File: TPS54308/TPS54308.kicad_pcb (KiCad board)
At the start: 2 copper layers, 30.5 x 15.2 mm, 14 parts, among them P1 CONN_01X04, P2 CONN_01X04, U1 TPS54308DDC

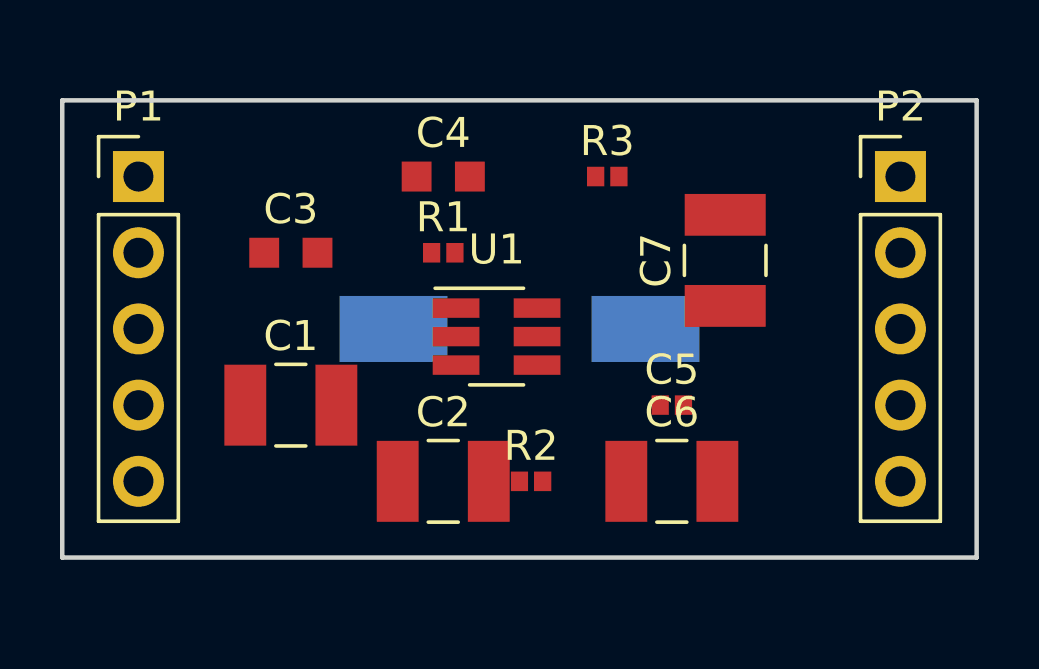
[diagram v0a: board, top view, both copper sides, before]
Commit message: placement draft
drafted placement of all components and started routing.
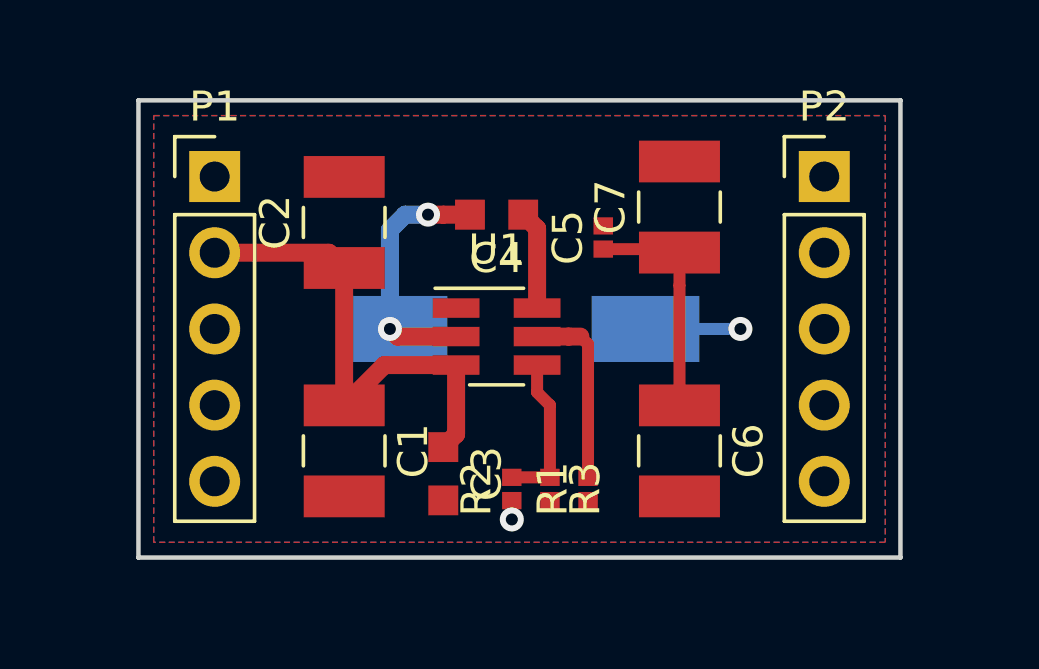
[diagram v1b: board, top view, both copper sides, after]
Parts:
- moved R3 10.6 mm to (110.2, 106.9), turned to 270 degrees
- moved C2 9.24 mm to (103.4, 98.1), turned to 90 degrees
- moved R1 9.24 mm to (111.5, 106.9), turned to 90 degrees
- moved C3 8.95 mm to (106.7, 106.4), turned to 270 degrees
- moved C5 6.04 mm to (112.0, 98.6), turned to 90 degrees
- moved P1 2.54 mm to (99.1, 96.5)
- moved P2 2.54 mm to (119.4, 96.5)
- moved C1 2.34 mm to (103.4, 105.7), turned to 270 degrees
- moved C7 2.34 mm to (114.6, 97.5)
- moved C4 2.18 mm to (108.5, 97.8), turned to 180 degrees
- moved C6 1.05 mm to (114.6, 105.7), turned to 270 degrees
- moved R2 0.69 mm to (109.0, 106.9), turned to 90 degrees
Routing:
- net VIN: track 0.00 -> 16.3 mm
- net VOUT: track 0.00 -> 11.5 mm, vias 0 -> 2
- net SW: track 0.00 -> 8.49 mm, vias 0 -> 2
- net EN: track 0.00 -> 6.24 mm
- net FB: track 0.00 -> 5.19 mm
- net BOOT: track 0.00 -> 3.31 mm
- added copper zone on B.Cu, net GND
- added copper zone on F.Cu, net GND
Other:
- board size 30.5 x 15.2 mm -> 25.4 x 15.2 mm

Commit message: size reduction
changed to 4pin pin headers, reduced board size, second placing attempt
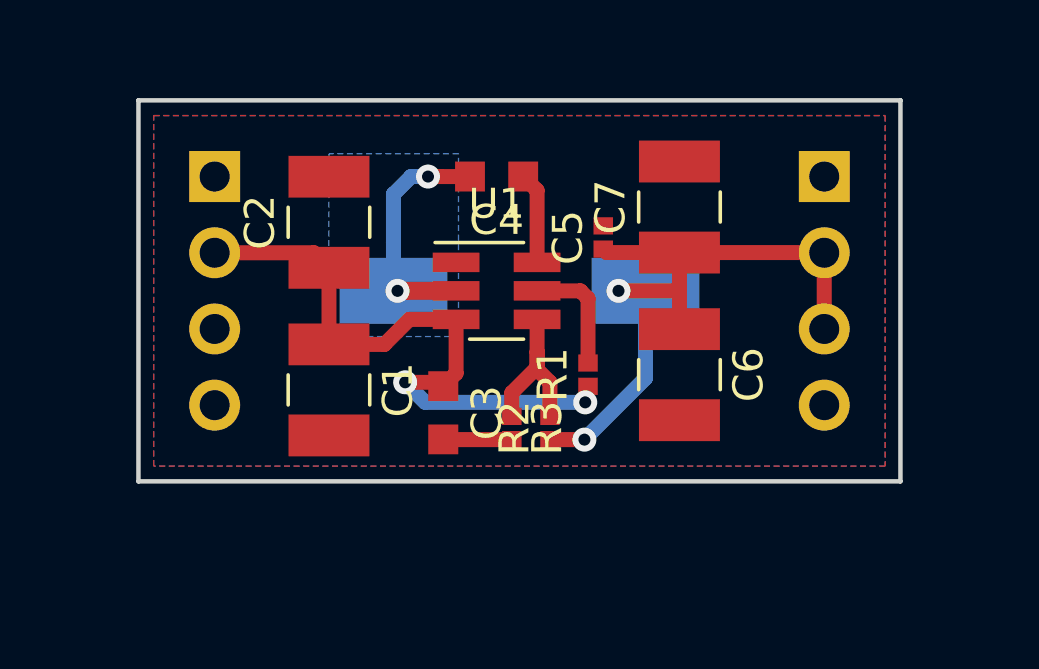
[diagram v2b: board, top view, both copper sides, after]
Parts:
- P1, P2: footprint Connector_PinHeader_2.54mm:PinHeader_1x05_P2.54mm_Vertical -> Connector_PinHeader_2.54mm:PinHeader_1x04_P2.54mm_Vertical; moved to B.Cu
- moved R1 3.81 mm to (111.5, 103.1)
- moved C6 2.54 mm to (114.6, 103.1)
- moved R2 2.40 mm to (110.2, 104.9)
- moved R3 2.40 mm to (109.0, 104.9)
- moved C1 2.09 mm to (102.9, 103.6)
- moved C3 2.03 mm to (106.7, 104.4)
- moved U1 1.52 mm to (108.5, 100.3)
- moved C4 1.27 mm to (108.5, 96.5)
- moved L1 1.27 mm to (109.2, 100.3)
- moved C2 0.51 mm to (102.9, 98.0)
- turned P1 to 180 degrees
- turned P2 to 180 degrees
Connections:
- P1 pad 3: EN -> GND
- P1 pad 4: GND -> EN
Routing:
- net VOUT: track 11.5 -> 22.7 mm
- net VIN: track 16.3 -> 21.8 mm, vias 0 -> 2
- net GND: track 0.00 -> 2.29 mm
- net EN: track 6.24 -> 3.96 mm
- net FB: track 5.19 -> 5.91 mm
- net SW: track 8.49 -> 7.97 mm
- added copper zone on B.Cu, net SW
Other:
- board size 25.4 x 15.2 mm -> 25.4 x 12.7 mm
- net class Default: trace_width 0.25 -> 0.5

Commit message: wired all connections
... additionally some copper fills and thermal vias
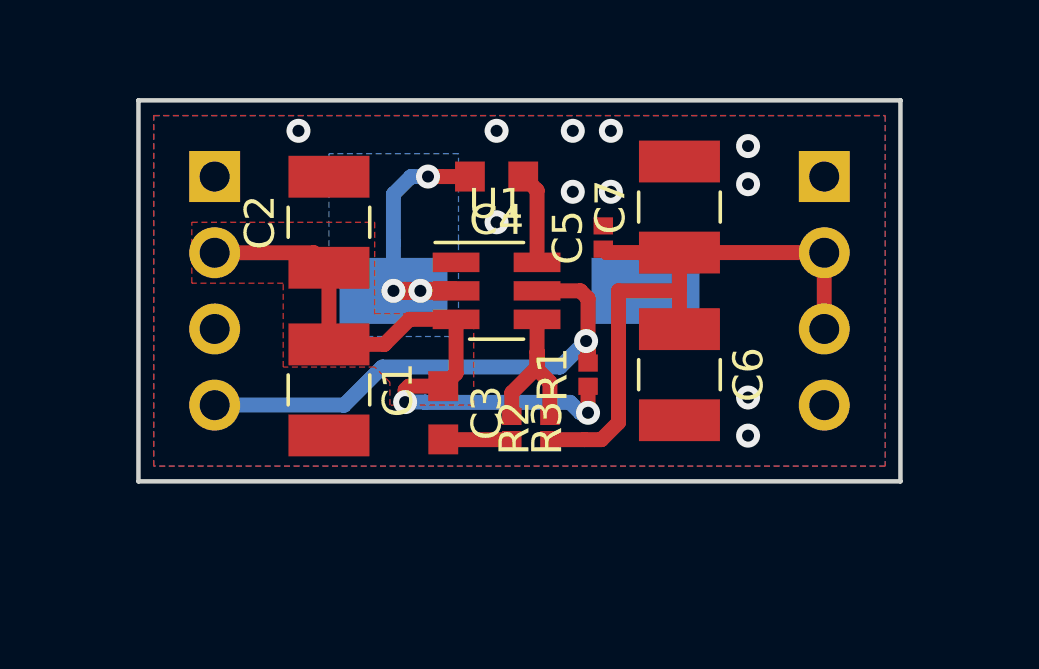
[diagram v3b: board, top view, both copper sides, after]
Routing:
- net EN: track 3.96 -> 18.1 mm, vias 0 -> 1
- net VIN: track 21.8 -> 22.7 mm
- net VOUT: vias 2 -> 0
- net SW: vias 2 -> 3
- net GND: vias 0 -> 11
- added copper zone on F.Cu, net VIN
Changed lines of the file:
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@@
   (general
     (thickness 1.6)
-    (drawings 4)
-    (tracks 55)
+    (drawings 6)
+    (tracks 79)
     (zones 0)
     (modules 14)
@@
     )
   )
+  (dimension 12.7 (width 0.3) (layer B.SilkS)
+    (gr_text "12,700 mm" (at 127.322 100.33 270) (layer B.SilkS)
+      (effects (font (size 1.5 1.5) (thickness 0.3)))
+    )
+    (feature1 (pts (xy 121.92 106.68) (xy 125.808421 106.68)))
+    (feature2 (pts (xy 121.92 93.98) (xy 125.808421 93.98)))
+    (crossbar (pts (xy 125.222 93.98) (xy 125.222 106.68)))
+    (arrow1a (pts (xy 125.222 106.68) (xy 124.635579 105.553496)))
+    (arrow1b (pts (xy 125.222 106.68) (xy 125.808421 105.553496)))
+    (arrow2a (pts (xy 125.222 93.98) (xy 124.635579 95.106504)))
+    (arrow2b (pts (xy 125.222 93.98) (xy 125.808421 95.106504)))
+  )
+  (dimension 25.4 (width 0.3) (layer B.SilkS)
+    (gr_text "25,400 mm" (at 109.22 113.86) (layer B.SilkS)
+      (effects (font (size 1.5 1.5) (thickness 0.3)))
+    )
+    (feature1 (pts (xy 121.92 106.68) (xy 121.92 112.346421)))
+    (feature2 (pts (xy 96.52 106.68) (xy 96.52 112.346421)))
+    (crossbar (pts (xy 96.52 111.76) (xy 121.92 111.76)))
+    (arrow1a (pts (xy 121.92 111.76) (xy 120.793496 112.346421)))
+    (arrow1b (pts (xy 121.92 111.76) (xy 120.793496 111.173579)))
+    (arrow2a (pts (xy 96.52 111.76) (xy 97.646504 112.346421)))
+    (arrow2b (pts (xy 96.52 111.76) (xy 97.646504 111.173579)))
+  )
   (gr_line (start 121.92 106.68) (end 96.52 106.68) (layer Edge.Cuts) (width 0.15))
   (gr_line (start 121.92 93.98) (end 121.92 106.68) (layer Edge.Cuts) (width 0.15))
@@
   (segment (start 107.108 100.33) (end 105.41 100.33) (width 0.6) (layer F.Cu) (net 1))
   (segment (start 105.41 100.33) (end 105.156 100.33) (width 0.6) (layer F.Cu) (net 1))
-  (via (at 105.156 100.33) (size 0.8) (drill 0.4) (layers F.Cu B.Cu) (net 1))
+  (via (at 105.02 100.33) (size 0.8) (drill 0.4) (layers F.Cu B.Cu) (net 1))
   (segment (start 107.5705 96.52) (end 106.573 96.52) (width 0.5) (layer F.Cu) (net 1))
   (segment (start 106.573 96.52) (end 106.172 96.52) (width 0.5) (layer F.Cu) (net 1))
@@
   (segment (start 105.606315 96.52) (end 105.02 97.106315) (width 0.5) (layer B.Cu) (net 1))
   (segment (start 106.172 96.52) (end 105.606315 96.52) (width 0.5) (layer B.Cu) (net 1))
+  (via (at 105.918 100.33) (size 0.8) (drill 0.4) (layers F.Cu B.Cu) (net 1))
   (segment (start 112.128 99.0535) (end 112.014 98.9395) (width 0.5) (layer F.Cu) (net 2))
   (segment (start 114.554 99.0535) (end 112.128 99.0535) (width 0.5) (layer F.Cu) (net 2))
@@
   (segment (start 114.554 100.251) (end 114.475 100.33) (width 0.5) (layer F.Cu) (net 2))
   (segment (start 114.554 99.0535) (end 114.554 100.251) (width 0.5) (layer F.Cu) (net 2))
-  (via (at 112.522 100.33) (size 0.8) (drill 0.4) (layers F.Cu B.Cu) (net 2))
   (segment (start 114.475 100.33) (end 112.522 100.33) (width 0.5) (layer F.Cu) (net 2))
   (segment (start 110.236 105.2895) (end 111.3855 105.2895) (width 0.5) (layer F.Cu) (net 2))
-  (via (at 111.3855 105.2895) (size 0.8) (drill 0.4) (layers F.Cu B.Cu) (net 2))
-  (segment (start 113.42 103.242) (end 113.42 100.33) (width 0.5) (layer B.Cu) (net 2))
-  (segment (start 111.3855 105.2895) (end 111.3725 105.2895) (width 0.5) (layer B.Cu) (net 2))
-  (segment (start 111.3725 105.2895) (end 113.42 103.242) (width 0.5) (layer B.Cu) (net 2))
   (segment (start 119.3735 99.0535) (end 119.38 99.06) (width 0.5) (layer F.Cu) (net 2))
   (segment (start 114.554 99.0535) (end 119.3735 99.0535) (width 0.5) (layer F.Cu) (net 2))
   (segment (start 119.38 101.6) (end 119.38 99.06) (width 0.5) (layer F.Cu) (net 2))
+  (segment (start 112.522 100.895685) (end 112.522 100.33) (width 0.5) (layer F.Cu) (net 2))
+  (segment (start 112.522 104.718685) (end 112.522 100.895685) (width 0.5) (layer F.Cu) (net 2))
+  (segment (start 111.951185 105.2895) (end 112.522 104.718685) (width 0.5) (layer F.Cu) (net 2))
+  (segment (start 111.3855 105.2895) (end 111.951185 105.2895) (width 0.5) (layer F.Cu) (net 2))
   (segment (start 107.108 103.0785) (end 106.68 103.5065) (width 0.5) (layer F.Cu) (net 3))
   (segment (start 107.108 101.28) (end 107.108 103.0785) (width 0.5) (layer F.Cu) (net 3))
@@
   (segment (start 102.87 102.1145) (end 104.72 102.1145) (width 0.5) (layer F.Cu) (net 3))
   (segment (start 104.72 102.1145) (end 105.5545 101.28) (width 0.5) (layer F.Cu) (net 3))
-  (via (at 111.412959 104.046959) (size 0.8) (drill 0.4) (layers F.Cu B.Cu) (net 3))
-  (segment (start 111.506 104.14) (end 111.412959 104.046959) (width 0.5) (layer F.Cu) (net 3))
-  (segment (start 111.506 103.5115) (end 111.412959 104.046959) (width 0.5) (layer F.Cu) (net 3))
-  (segment (start 111.412959 104.046959) (end 106.078959 104.046959) (width 0.5) (layer B.Cu) (net 3))
-  (via (at 105.41 103.378) (size 0.8) (drill 0.4) (layers F.Cu B.Cu) (net 3))
-  (segment (start 106.078959 104.046959) (end 105.41 103.378) (width 0.5) (layer B.Cu) (net 3))
-  (segment (start 106.5515 103.378) (end 106.68 103.5065) (width 0.5) (layer F.Cu) (net 3))
-  (segment (start 105.41 103.378) (end 106.5515 103.378) (width 0.5) (layer F.Cu) (net 3))
   (segment (start 102.3685 99.06) (end 102.87 99.5615) (width 0.5) (layer F.Cu) (net 3))
   (segment (start 99.06 99.06) (end 102.3685 99.06) (width 0.5) (layer F.Cu) (net 3))
+  (via (at 105.41 104.0384) (size 0.8) (drill 0.4) (layers F.Cu B.Cu) (net 3))
+  (segment (start 105.41 104.0384) (end 105.41 103.632) (width 0.5) (layer F.Cu) (net 3))
+  (segment (start 105.5355 103.5065) (end 106.68 103.5065) (width 0.5) (layer F.Cu) (net 3))
+  (segment (start 105.41 103.632) (end 105.5355 103.5065) (width 0.5) (layer F.Cu) (net 3))
+  (via (at 111.506 104.394) (size 0.8) (drill 0.4) (layers F.Cu B.Cu) (net 3))
+  (segment (start 111.506 103.5115) (end 111.506 104.394) (width 0.5) (layer F.Cu) (net 3))
+  (segment (start 111.506 104.14) (end 111.506 104.394) (width 0.5) (layer F.Cu) (net 3))
+  (segment (start 106.0704 104.0384) (end 105.41 104.0384) (width 0.5) (layer B.Cu) (net 3))
+  (segment (start 106.078959 104.046959) (end 106.0704 104.0384) (width 0.5) (layer B.Cu) (net 3))
+  (segment (start 110.904959 104.046959) (end 106.078959 104.046959) (width 0.5) (layer B.Cu) (net 3))
+  (segment (start 111.506 104.394) (end 111.252 104.394) (width 0.5) (layer B.Cu) (net 3))
+  (segment (start 111.252 104.394) (end 110.904959 104.046959) (width 0.5) (layer B.Cu) (net 3))
   (segment (start 111.252 100.33) (end 109.808 100.33) (width 0.5) (layer F.Cu) (net 4))
   (segment (start 111.506 100.584) (end 111.252 100.33) (width 0.5) (layer F.Cu) (net 4))
   (segment (start 111.506 102.7365) (end 111.506 100.584) (width 0.5) (layer F.Cu) (net 4))
+  (via (at 111.441759 102.002915) (size 0.8) (drill 0.4) (layers F.Cu B.Cu) (net 4))
+  (segment (start 111.479999 101.964675) (end 111.441759 102.002915) (width 0.5) (layer B.Cu) (net 4))
+  (segment (start 111.479999 101.880001) (end 111.479999 101.964675) (width 0.5) (layer B.Cu) (net 4))
+  (segment (start 111.506 102.067156) (end 111.441759 102.002915) (width 0.5) (layer F.Cu) (net 4))
+  (segment (start 111.506 102.7365) (end 111.506 102.067156) (width 0.5) (layer F.Cu) (net 4))
+  (segment (start 110.574674 102.87) (end 111.441759 102.002915) (width 0.5) (layer B.Cu) (net 4))
+  (segment (start 104.648 102.87) (end 110.574674 102.87) (width 0.5) (layer B.Cu) (net 4))
+  (segment (start 99.06 104.14) (end 103.378 104.14) (width 0.5) (layer B.Cu) (net 4))
+  (segment (start 103.378 104.14) (end 104.648 102.87) (width 0.5) (layer B.Cu) (net 4))
   (segment (start 109.808 102.885) (end 109.808 102.362) (width 0.5) (layer F.Cu) (net 5))
   (segment (start 108.966 103.727) (end 109.808 102.885) (width 0.5) (layer F.Cu) (net 5))
@@
   (segment (start 106.688 105.2895) (end 106.68 105.2815) (width 0.5) (layer F.Cu) (net 6))
   (segment (start 108.966 105.2895) (end 106.688 105.2895) (width 0.5) (layer F.Cu) (net 6))
+  (via (at 116.84 105.156) (size 0.8) (drill 0.4) (layers F.Cu B.Cu) (net 6))
+  (via (at 116.84 103.886) (size 0.8) (drill 0.4) (layers F.Cu B.Cu) (net 6))
+  (via (at 116.84 95.504) (size 0.8) (drill 0.4) (layers F.Cu B.Cu) (net 6))
+  (via (at 116.84 96.774) (size 0.8) (drill 0.4) (layers F.Cu B.Cu) (net 6))
+  (via (at 108.458 98.044) (size 0.8) (drill 0.4) (layers F.Cu B.Cu) (net 6))
+  (via (at 108.458 94.996) (size 0.8) (drill 0.4) (layers F.Cu B.Cu) (net 6))
+  (via (at 110.998 94.996) (size 0.8) (drill 0.4) (layers F.Cu B.Cu) (net 6))
+  (via (at 110.998 97.028) (size 0.8) (drill 0.4) (layers F.Cu B.Cu) (net 6))
+  (via (at 112.268 94.996) (size 0.8) (drill 0.4) (layers F.Cu B.Cu) (net 6))
+  (via (at 112.268 97.028) (size 0.8) (drill 0.4) (layers F.Cu B.Cu) (net 6))
+  (via (at 101.854 94.996) (size 0.8) (drill 0.4) (layers F.Cu B.Cu) (net 6))
   (segment (start 109.808 96.9825) (end 109.3455 96.52) (width 0.5) (layer F.Cu) (net 7))
   (segment (start 109.808 99.38) (end 109.808 96.9825) (width 0.5) (layer F.Cu) (net 7))
@@
       )
     )
+  )
+  (zone (net 3) (net_name VIN) (layer F.Cu) (hatch edge 0.508)
+    (priority 2)
+    (connect_pads yes (clearance 0.508))
+    (min_thickness 0.254)
+    (fill yes (arc_segments 16) (thermal_gap 0.508) (thermal_bridge_width 0.508))
+    (polygon
+      (pts
+        (xy 98.298 98.044) (xy 104.394 98.044) (xy 104.394 101.092) (xy 107.696 101.092) (xy 107.696 104.14)
+        (xy 104.902 104.14) (xy 104.902 103.378) (xy 104.394 102.87) (xy 101.346 102.87) (xy 101.346 100.076)
+        (xy 98.298 100.076)
+      )
+    )

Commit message: Silkscreen improvement
Made references readable
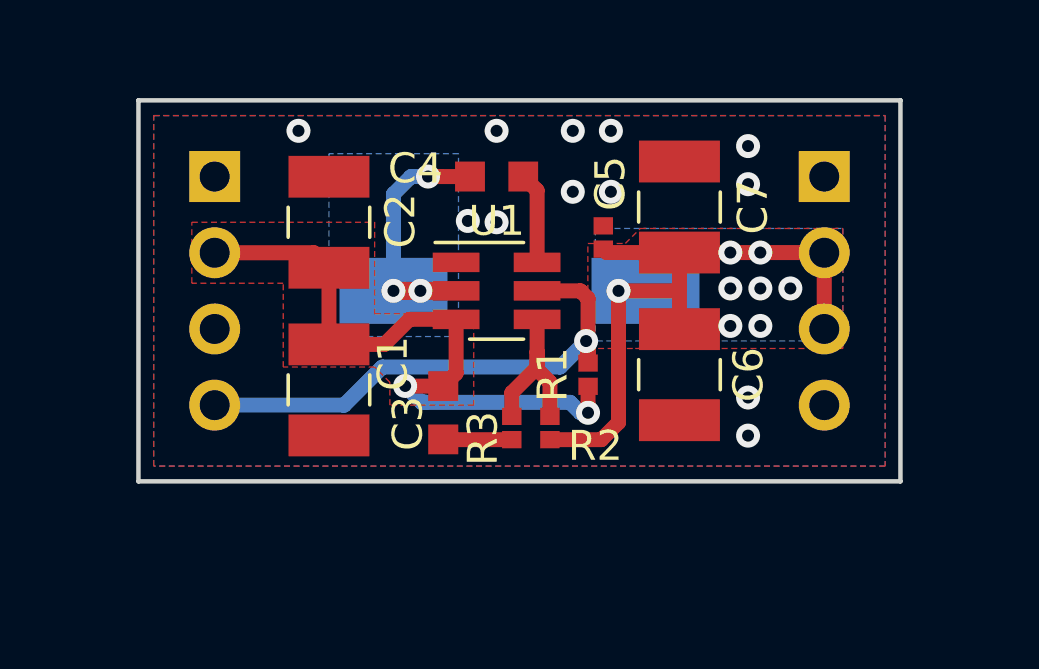
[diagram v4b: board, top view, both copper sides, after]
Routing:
- net VOUT: vias 0 -> 8
- net GND: vias 11 -> 12
- added copper zone on B.Cu, net VOUT
- added copper zone on F.Cu, net VOUT
